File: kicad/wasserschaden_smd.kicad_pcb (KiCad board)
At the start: 2 copper layers, 49.5 x 33 mm, 19 parts, among them J1 valve out, J2 12V in, J3 sense, U1 stepdown, U2 WeMos_mini, U3 DS18B20

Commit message: small rerouting
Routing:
- net +3V3: track 7.86 -> 0.88 mm
- net Net-(R6-Pad2): track 41.2 -> 43.6 mm
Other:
- board text added: "5"
- board text added: "info"
- board text added: "power"
- board text added: "valve"
- board text added: "version"
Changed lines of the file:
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@@
   (general
     (thickness 1.6)
-    (drawings 10)
-    (tracks 73)
+    (drawings 17)
+    (tracks 68)
     (zones 0)
     (modules 19)
@@
     (pad_drill 0.6)
     (pad_to_mask_clearance 0)
+    (solder_mask_min_width 0.25)
     (aux_axis_origin 0 0)
     (visible_elements FFFFFF7F)
@@
       (outputformat 1)
       (mirror false)
-      (drillshape 1)
+      (drillshape 0)
       (scaleselection 1)
-      (outputdirectory ""))
+      (outputdirectory "smd/"))
   )
   (net 0 "")
@@
     (descr "LED, diameter 3.0mm, 2 pins")
     (tags "LED diameter 3.0mm 2 pins")
-    (fp_text reference D4 (at 1.27 -2.96) (layer F.SilkS)
+    (fp_text reference D4 (at 1.27 -1.27) (layer F.SilkS)
       (effects (font (size 1 1) (thickness 0.15)))
     )
@@
     (descr "LED, diameter 3.0mm, 2 pins")
     (tags "LED diameter 3.0mm 2 pins")
-    (fp_text reference D2 (at 1.27 -2.96) (layer F.SilkS)
+    (fp_text reference D2 (at 1.27 -1.27) (layer F.SilkS)
       (effects (font (size 1 1) (thickness 0.15)))
     )
@@
     (descr "LED, diameter 3.0mm, 2 pins")
     (tags "LED diameter 3.0mm 2 pins")
-    (fp_text reference D3 (at 1.27 -2.96) (layer F.SilkS)
+    (fp_text reference D3 (at 1.27 -1.27) (layer F.SilkS)
       (effects (font (size 1 1) (thickness 0.15)))
     )
@@
     )
   )
+  (gr_text version (at 121.666 41.0845 90) (layer F.SilkS)
+    (effects (font (size 0.3 0.3) (thickness 0.05)))
+  )
+  (gr_text "- +\n" (at 137.795 67.31) (layer F.SilkS)
+    (effects (font (size 1.5 1.5) (thickness 0.3)))
+  )
+  (gr_text power (at 142.875 71.12) (layer F.SilkS)
+    (effects (font (size 1 1) (thickness 0.2)))
+  )
+  (gr_text info (at 137.795 71.12) (layer F.SilkS)
+    (effects (font (size 1 1) (thickness 0.2)))
+  )
+  (gr_text valve (at 132.715 71.12) (layer F.SilkS)
+    (effects (font (size 1 1) (thickness 0.2)))
+  )
+  (gr_text 5 (at 144.78 55.245 90) (layer B.SilkS)
+    (effects (font (size 40 33) (thickness 6)))
+  )
+  (gr_text 5 (at 122.4915 41.148) (layer F.SilkS)
+    (effects (font (size 1.5 1.5) (thickness 0.3)))
+  )
   (gr_text "-   +" (at 165.1 45.72 90) (layer F.SilkS)
     (effects (font (size 1.5 1.5) (thickness 0.3)))
@@
   (segment (start 125.56 49.53) (end 124.29 48.26) (width 0.25) (layer F.Cu) (net 4))
   (segment (start 125.73 49.53) (end 125.56 49.53) (width 0.25) (layer F.Cu) (net 4))
-  (segment (start 122.09 44.45) (end 122.09 50.165) (width 0.25) (layer F.Cu) (net 9))
-  (segment (start 122.09 50.165) (end 122.09 55.88) (width 0.25) (layer F.Cu) (net 9))
-  (via (at 122.09 50.165) (size 0.8) (drill 0.4) (layers F.Cu B.Cu) (net 9))
   (segment (start 124.46 63.67) (end 124.29 63.5) (width 0.25) (layer F.Cu) (net 5))
-  (segment (start 137.16 41.366998) (end 137.16 43.18) (width 0.25) (layer F.Cu) (net 5))
-  (segment (start 137.16 41.366998) (end 137.16 40.64) (width 0.25) (layer F.Cu) (net 5))
-  (segment (start 139.7 40.64) (end 139.7 43.18) (width 0.25) (layer F.Cu) (net 5))
-  (segment (start 134.62 42.543) (end 134.62 40.64) (width 0.25) (layer F.Cu) (net 5))
   (segment (start 134.62 42.543) (end 134.62 43.18) (width 0.25) (layer F.Cu) (net 5))
   (segment (start 125.14 52.07) (end 124.29 52.07) (width 0.25) (layer F.Cu) (net 6))
@@
   (segment (start 138.43 68.58) (end 139.065 69.215) (width 0.25) (layer B.Cu) (net 8))
   (segment (start 138.43 64.77) (end 138.43 68.58) (width 0.25) (layer B.Cu) (net 8))
+  (segment (start 122.09 44.45) (end 122.09 50.165) (width 0.25) (layer F.Cu) (net 9))
+  (segment (start 122.09 50.165) (end 122.09 55.88) (width 0.25) (layer F.Cu) (net 9))
+  (via (at 122.09 50.165) (size 0.8) (drill 0.4) (layers F.Cu B.Cu) (net 9))
   (segment (start 130.81 59.69) (end 135.89 64.77) (width 0.25) (layer F.Cu) (net 10))
   (segment (start 124.29 59.69) (end 130.81 59.69) (width 0.25) (layer F.Cu) (net 10))
@@
   (segment (start 146.4056 41.5544) (end 146.05 41.91) (width 0.25) (layer F.Cu) (net 12))
   (segment (start 151.13 41.5544) (end 146.4056 41.5544) (width 0.25) (layer F.Cu) (net 12))
-  (segment (start 121.94 63.5) (end 120.015 61.575) (width 0.25) (layer F.Cu) (net 13))
-  (segment (start 122.09 63.5) (end 121.94 63.5) (width 0.25) (layer F.Cu) (net 13))
-  (segment (start 120.015 61.575) (end 120.015 44.889998) (width 0.25) (layer F.Cu) (net 13))
-  (segment (start 132.450001 42.809999) (end 133.35 41.91) (width 0.25) (layer F.Cu) (net 13))
-  (segment (start 121.229999 43.674999) (end 131.585001 43.674999) (width 0.25) (layer F.Cu) (net 13))
-  (segment (start 131.585001 43.674999) (end 132.450001 42.809999) (width 0.25) (layer F.Cu) (net 13))
-  (segment (start 120.015 44.889998) (end 121.229999 43.674999) (width 0.25) (layer F.Cu) (net 13))
   (segment (start 125.095 67.800787) (end 125.095 69.215) (width 0.25) (layer F.Cu) (net 13))
   (segment (start 125.095 66.355) (end 125.095 67.800787) (width 0.25) (layer F.Cu) (net 13))
   (segment (start 122.24 63.5) (end 125.095 66.355) (width 0.25) (layer F.Cu) (net 13))
   (segment (start 122.09 63.5) (end 122.24 63.5) (width 0.25) (layer F.Cu) (net 13))
+  (segment (start 120.015 42.545) (end 121.92 40.64) (width 0.25) (layer F.Cu) (net 13))
+  (segment (start 120.015 61.575) (end 120.015 42.545) (width 0.25) (layer F.Cu) (net 13))
+  (segment (start 132.08 40.64) (end 133.35 41.91) (width 0.25) (layer F.Cu) (net 13))
+  (segment (start 122.09 63.5) (end 121.94 63.5) (width 0.25) (layer F.Cu) (net 13))
+  (segment (start 121.94 63.5) (end 120.015 61.575) (width 0.25) (layer F.Cu) (net 13))
+  (segment (start 121.92 40.64) (end 132.08 40.64) (width 0.25) (layer F.Cu) (net 13))
   (zone (net 9) (net_name GND) (layer B.Cu) (hatch edge 0.508)
     (connect_pads (clearance 0.508))

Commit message: pcb v7
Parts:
- D1: footprint Diodes_THT:D_A-405_P7.62mm_Horizontal -> Diodes_SMD:D_SMA_Handsoldering
- moved D1 2.59 mm to (148.0, 61.0)
- moved U1 1.28 mm to (139.0, 51.0)
- moved IRFZ44N1 0.21 mm to (150.0, 70.0)
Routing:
- net Net-(D1-Pad2): track 26.3 -> 27.9 mm
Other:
- board text added: "7"
- board text removed: "5"
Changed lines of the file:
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@@
     (thickness 1.6)
     (drawings 17)
-    (tracks 68)
+    (tracks 69)
     (zones 0)
     (modules 19)
@@
       (net 5 +3V3))
   )
-  (module custom:irlz44n_vertical (layer F.Cu)
-    (at 149.86 69.85 270)
-    (fp_text reference IRFZ44N1 (at -2.286 0 180) (layer F.SilkS)
-      (effects (font (size 1 1) (thickness 0.15)))
-    )
-    (fp_text value " " (at 0 -0.5 270) (layer F.Fab)
-      (effects (font (size 1 1) (thickness 0.15)))
-    )
-    (fp_poly (pts (xy -1.651 -3.556) (xy -1.651 3.556) (xy -1.016 3.556) (xy -1.016 -3.556)) (layer F.SilkS) (width 0.15))
-    (pad 1 thru_hole circle (at 0 -2.54 270) (size 2 2) (drill oval 0.762 1) (layers *.Cu *.Mask)
-      (net 9 GND))
-    (pad 3 thru_hole circle (at 0 0 270) (size 2 2) (drill oval 0.762 1) (layers *.Cu *.Mask)
-      (net 1 "Net-(D1-Pad2)"))
-    (pad 2 thru_hole circle (at 0 2.54 270) (size 2 2) (drill oval 0.762 1) (layers *.Cu *.Mask)
-      (net 3 "Net-(D2-Pad2)"))
-  )
-  (module Diodes_THT:D_A-405_P7.62mm_Horizontal (layer F.Cu)
-    (at 145.415 60.96)
-    (descr "D, A-405 series, Axial, Horizontal, pin pitch=7.62mm, , length*diameter=5.2*2.7mm^2, , http://www.diodes.com/_files/packages/A-405.pdf")
-    (tags "D A-405 series Axial Horizontal pin pitch 7.62mm  length 5.2mm diameter 2.7mm")
-    (fp_text reference D1 (at 3.81 -2.41) (layer F.SilkS)
-      (effects (font (size 1 1) (thickness 0.15)))
-    )
-    (fp_text value " " (at 3.81 2.41) (layer F.Fab)
-      (effects (font (size 1 1) (thickness 0.15)))
-    )
-    (fp_line (start 8.8 -1.7) (end -1.15 -1.7) (layer F.CrtYd) (width 0.05))
-    (fp_line (start 8.8 1.7) (end 8.8 -1.7) (layer F.CrtYd) (width 0.05))
-    (fp_line (start -1.15 1.7) (end 8.8 1.7) (layer F.CrtYd) (width 0.05))
-    (fp_line (start -1.15 -1.7) (end -1.15 1.7) (layer F.CrtYd) (width 0.05))
-    (fp_line (start 1.99 -1.41) (end 1.99 1.41) (layer F.SilkS) (width 0.12))
-    (fp_line (start 6.54 0) (end 6.47 0) (layer F.SilkS) (width 0.12))
-    (fp_line (start 1.08 0) (end 1.15 0) (layer F.SilkS) (width 0.12))
-    (fp_line (start 6.47 -1.41) (end 1.15 -1.41) (layer F.SilkS) (width 0.12))
-    (fp_line (start 6.47 1.41) (end 6.47 -1.41) (layer F.SilkS) (width 0.12))
-    (fp_line (start 1.15 1.41) (end 6.47 1.41) (layer F.SilkS) (width 0.12))
-    (fp_line (start 1.15 -1.41) (end 1.15 1.41) (layer F.SilkS) (width 0.12))
-    (fp_line (start 1.99 -1.35) (end 1.99 1.35) (layer F.Fab) (width 0.1))
-    (fp_line (start 7.62 0) (end 6.41 0) (layer F.Fab) (width 0.1))
-    (fp_line (start 0 0) (end 1.21 0) (layer F.Fab) (width 0.1))
-    (fp_line (start 6.41 -1.35) (end 1.21 -1.35) (layer F.Fab) (width 0.1))
-    (fp_line (start 6.41 1.35) (end 6.41 -1.35) (layer F.Fab) (width 0.1))
-    (fp_line (start 1.21 1.35) (end 6.41 1.35) (layer F.Fab) (width 0.1))
-    (fp_line (start 1.21 -1.35) (end 1.21 1.35) (layer F.Fab) (width 0.1))
-    (fp_text user %R (at 3.81 0) (layer F.Fab)
-      (effects (font (size 1 1) (thickness 0.15)))
-    )
-    (pad 2 thru_hole oval (at 7.62 0) (size 1.8 1.8) (drill 0.9) (layers *.Cu *.Mask)
-      (net 1 "Net-(D1-Pad2)"))
-    (pad 1 thru_hole rect (at 0 0) (size 1.8 1.8) (drill 0.9) (layers *.Cu *.Mask)
-      (net 2 +12V))
-    (model ${KISYS3DMOD}/Diodes_THT.3dshapes/D_A-405_P7.62mm_Horizontal.wrl
-      (at (xyz 0 0 0))
-      (scale (xyz 0.393701 0.393701 0.393701))
-      (rotate (xyz 0 0 0))
-    )
-  )
   (module LEDs:LED_D3.0mm (layer F.Cu)
     (at 131.445 69.215)
@@
   )
   (module custom:stepdown (layer F.Cu)
-    (at 139.7 52.07 180)
+    (at 139 51 180)
     (fp_text reference U1 (at 0.254 4.318 180) (layer F.SilkS)
       (effects (font (size 1 1) (thickness 0.15)))
@@
     )
   )
+  (module Diodes_SMD:D_SMA_Handsoldering (layer F.Cu)
+    (at 148 61)
+    (descr "Diode SMA (DO-214AC) Handsoldering")
+    (tags "Diode SMA (DO-214AC) Handsoldering")
+    (attr smd)
+    (fp_text reference D1 (at 0 -2.5) (layer F.SilkS)
+      (effects (font (size 1 1) (thickness 0.15)))
+    )
+    (fp_text value " " (at 0 2.6) (layer F.Fab)
+      (effects (font (size 1 1) (thickness 0.15)))
+    )
+    (fp_line (start -4.4 -1.65) (end 2.5 -1.65) (layer F.SilkS) (width 0.12))
+    (fp_line (start -4.4 1.65) (end 2.5 1.65) (layer F.SilkS) (width 0.12))
+    (fp_line (start -0.64944 0.00102) (end 0.50118 -0.79908) (layer F.Fab) (width 0.1))
+    (fp_line (start -0.64944 0.00102) (end 0.50118 0.75032) (layer F.Fab) (width 0.1))
+    (fp_line (start 0.50118 0.75032) (end 0.50118 -0.79908) (layer F.Fab) (width 0.1))
+    (fp_line (start -0.64944 -0.79908) (end -0.64944 0.80112) (layer F.Fab) (width 0.1))
+    (fp_line (start 0.50118 0.00102) (end 1.4994 0.00102) (layer F.Fab) (width 0.1))
+    (fp_line (start -0.64944 0.00102) (end -1.55114 0.00102) (layer F.Fab) (width 0.1))
+    (fp_line (start -4.5 1.75) (end -4.5 -1.75) (layer F.CrtYd) (width 0.05))
+    (fp_line (start 4.5 1.75) (end -4.5 1.75) (layer F.CrtYd) (width 0.05))
+    (fp_line (start 4.5 -1.75) (end 4.5 1.75) (layer F.CrtYd) (width 0.05))
+    (fp_line (start -4.5 -1.75) (end 4.5 -1.75) (layer F.CrtYd) (width 0.05))
+    (fp_line (start 2.3 -1.5) (end -2.3 -1.5) (layer F.Fab) (width 0.1))
+    (fp_line (start 2.3 -1.5) (end 2.3 1.5) (layer F.Fab) (width 0.1))
+    (fp_line (start -2.3 1.5) (end -2.3 -1.5) (layer F.Fab) (width 0.1))
+    (fp_line (start 2.3 1.5) (end -2.3 1.5) (layer F.Fab) (width 0.1))
+    (fp_line (start -4.4 -1.65) (end -4.4 1.65) (layer F.SilkS) (width 0.12))
+    (fp_text user %R (at 0 -2.5) (layer F.Fab)
+      (effects (font (size 1 1) (thickness 0.15)))
+    )
+    (pad 2 smd rect (at 2.5 0) (size 3.5 1.8) (layers F.Cu F.Paste F.Mask)
+      (net 1 "Net-(D1-Pad2)"))
+    (pad 1 smd rect (at -2.5 0) (size 3.5 1.8) (layers F.Cu F.Paste F.Mask)
+      (net 2 +12V))
+    (model ${KISYS3DMOD}/Diodes_SMD.3dshapes/D_SMA.wrl
+      (at (xyz 0 0 0))
+      (scale (xyz 1 1 1))
+      (rotate (xyz 0 0 0))
+    )
+  )
+  (module custom:irlz44n_vertical (layer F.Cu)
+    (at 150 70 270)
+    (fp_text reference IRFZ44N1 (at 1.651 0 180) (layer F.SilkS)
+      (effects (font (size 1 1) (thickness 0.15)))
+    )
+    (fp_text value " " (at 0 -0.5 270) (layer F.Fab)
+      (effects (font (size 1 1) (thickness 0.15)))
+    )
+    (fp_poly (pts (xy -1.651 -3.556) (xy -1.651 3.556) (xy -1.016 3.556) (xy -1.016 -3.556)) (layer F.SilkS) (width 0.15))
+    (pad 2 thru_hole circle (at 0 2.54 270) (size 2 2) (drill oval 0.762 1) (layers *.Cu *.Mask)
+      (net 3 "Net-(D2-Pad2)"))
+    (pad 3 thru_hole circle (at 0 0 270) (size 2 2) (drill oval 0.762 1) (layers *.Cu *.Mask)
+      (net 1 "Net-(D1-Pad2)"))
+    (pad 1 thru_hole circle (at 0 -2.54 270) (size 2 2) (drill oval 0.762 1) (layers *.Cu *.Mask)
+      (net 9 GND))
+  )
   (gr_text version (at 121.666 41.0845 90) (layer F.SilkS)
     (effects (font (size 0.3 0.3) (thickness 0.05)))
@@
     (effects (font (size 1 1) (thickness 0.2)))
   )
-  (gr_text 5 (at 144.78 55.245 90) (layer B.SilkS)
-    (effects (font (size 40 33) (thickness 6)))
+  (gr_text 7 (at 144.78 55.245 90) (layer B.SilkS)
+    (effects (font (size 40 33) (thickness 6)) (justify mirror))
   )
-  (gr_text 5 (at 122.4915 41.148) (layer F.SilkS)
+  (gr_text 7 (at 122.4915 41.148) (layer F.SilkS)
     (effects (font (size 1.5 1.5) (thickness 0.3)))
   )
@@
   (gr_arc (start 163.83 43.18) (end 167.64 43.18) (angle -90) (layer Edge.Cuts) (width 0.1))
   (gr_arc (start 121.92 43.18) (end 121.92 39.37) (angle -90) (layer Edge.Cuts) (width 0.1))
-  (segment (start 155.575 58.42) (end 153.035 60.96) (width 0.6) (layer F.Cu) (net 1))
+  (segment (start 155.575 58.42) (end 152.995 61) (width 0.6) (layer F.Cu) (net 1))
   (segment (start 161.29 48.26) (end 155.575 53.975) (width 0.6) (layer F.Cu) (net 1))
+  (segment (start 152.995 61) (end 150.5 61) (width 0.6) (layer F.Cu) (net 1))
   (segment (start 155.575 53.975) (end 155.575 58.42) (width 0.6) (layer F.Cu) (net 1))
-  (segment (start 149.86 64.135) (end 153.035 60.96) (width 0.6) (layer B.Cu) (net 1))
-  (segment (start 149.86 69.85) (end 149.86 64.135) (width 0.6) (layer B.Cu) (net 1))
+  (segment (start 150.5 69.5) (end 150 70) (width 0.6) (layer F.Cu) (net 1))
+  (segment (start 150.5 61) (end 150.5 69.5) (width 0.6) (layer F.Cu) (net 1))
   (segment (start 140.97 64.77) (end 143.51 67.31) (width 0.25) (layer B.Cu) (net 3))
   (segment (start 144.78 67.31) (end 147.32 69.85) (width 0.25) (layer B.Cu) (net 3))

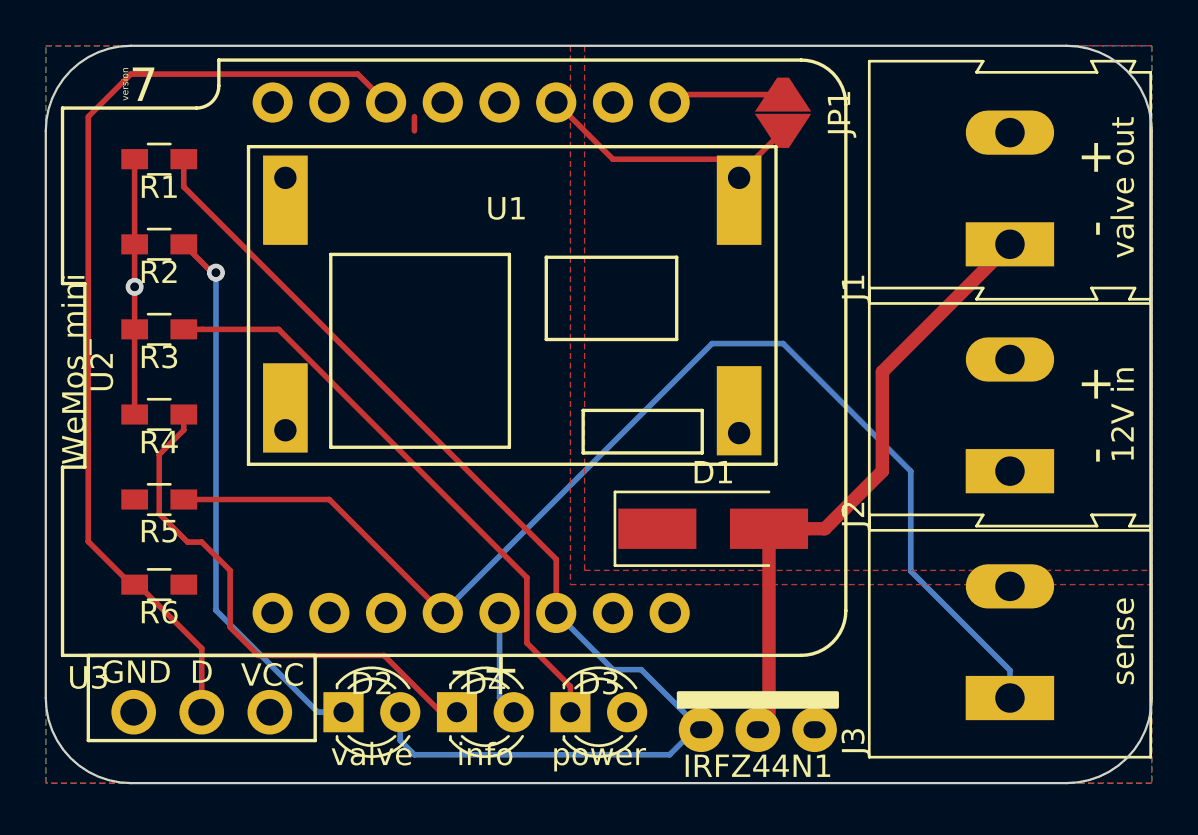
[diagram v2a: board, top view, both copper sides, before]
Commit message: fixed traces near pads
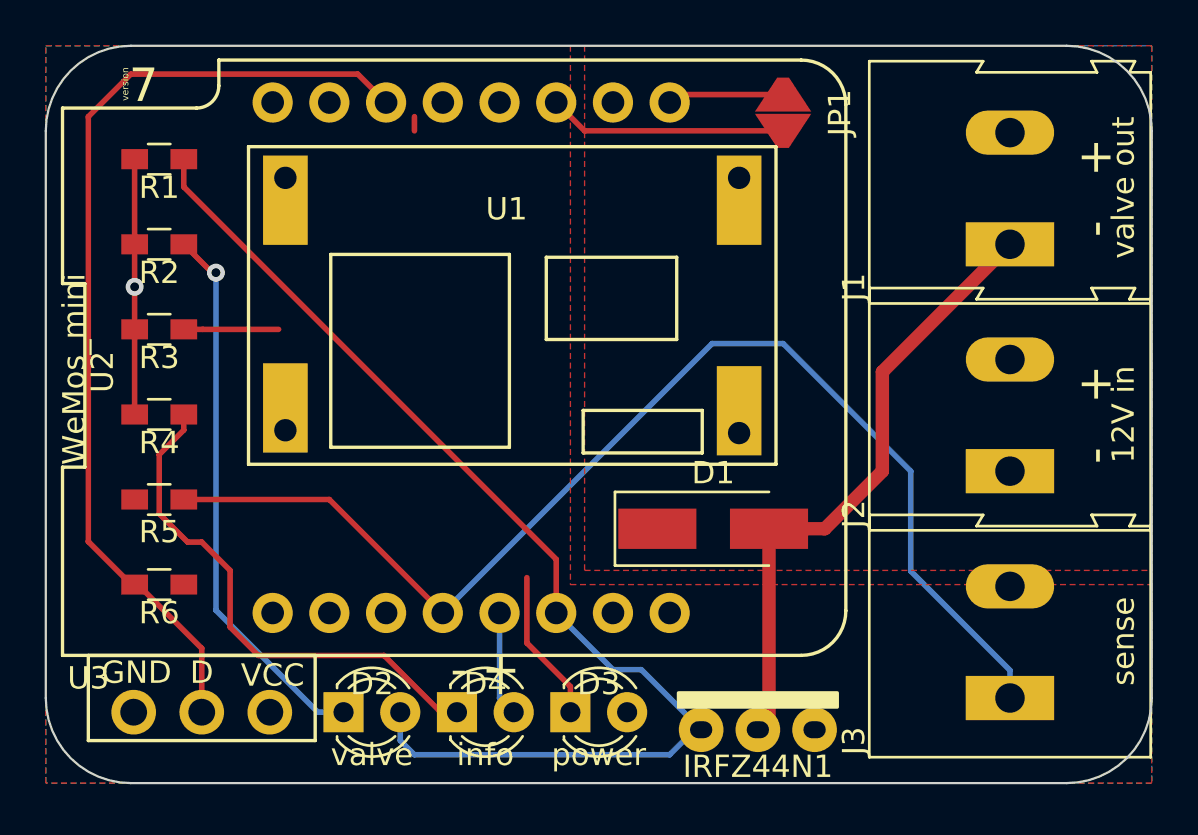
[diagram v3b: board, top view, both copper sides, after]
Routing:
- net Net-(D3-Pad1): track 26.8 -> 11.1 mm
- net Net-(JP1-Pad1): track 11.7 -> 10.7 mm
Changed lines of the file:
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@@
     (thickness 1.6)
     (drawings 17)
-    (tracks 69)
+    (tracks 67)
     (zones 0)
     (modules 19)
@@
   (segment (start 124.46 63.67) (end 124.29 63.5) (width 0.25) (layer F.Cu) (net 5))
   (segment (start 134.62 42.543) (end 134.62 43.18) (width 0.25) (layer F.Cu) (net 5))
-  (segment (start 125.14 52.07) (end 124.29 52.07) (width 0.25) (layer F.Cu) (net 6))
   (segment (start 128.537002 52.07) (end 125.14 52.07) (width 0.25) (layer F.Cu) (net 6))
-  (segment (start 139.655001 63.187999) (end 128.537002 52.07) (width 0.25) (layer F.Cu) (net 6))
+  (segment (start 125.14 52.07) (end 124.29 52.07) (width 0.25) (layer F.Cu) (net 6))
   (segment (start 139.655001 66.115001) (end 139.655001 63.187999) (width 0.25) (layer F.Cu) (net 6))
   (segment (start 141.605 68.065) (end 139.655001 66.115001) (width 0.25) (layer F.Cu) (net 6))
@@
   (segment (start 135.89 64.77) (end 147.955 52.705) (width 0.25) (layer B.Cu) (net 10))
   (segment (start 147.955 52.705) (end 151.13 52.705) (width 0.25) (layer B.Cu) (net 10))
-  (segment (start 149.86 44.45) (end 151.13 43.18) (width 0.25) (layer F.Cu) (net 11))
-  (segment (start 140.97 41.91) (end 143.51 44.45) (width 0.25) (layer F.Cu) (net 11))
-  (segment (start 143.51 44.45) (end 149.86 44.45) (width 0.25) (layer F.Cu) (net 11))
+  (segment (start 142.24 43.18) (end 140.97 41.91) (width 0.25) (layer F.Cu) (net 11))
+  (segment (start 151.13 43.18) (end 142.24 43.18) (width 0.25) (layer F.Cu) (net 11))
   (segment (start 146.4056 41.5544) (end 146.05 41.91) (width 0.25) (layer F.Cu) (net 12))
   (segment (start 151.13 41.5544) (end 146.4056 41.5544) (width 0.25) (layer F.Cu) (net 12))
